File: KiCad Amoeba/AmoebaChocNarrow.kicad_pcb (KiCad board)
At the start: 2 copper layers, 12.5 x 30 mm, 10 parts, among them J1 Conn_01x01_Pin, J2 Conn_01x01_Pin, J3 Conn_01x01_Pin, J4 Conn_01x01_Pin, SW1 SW_SPST

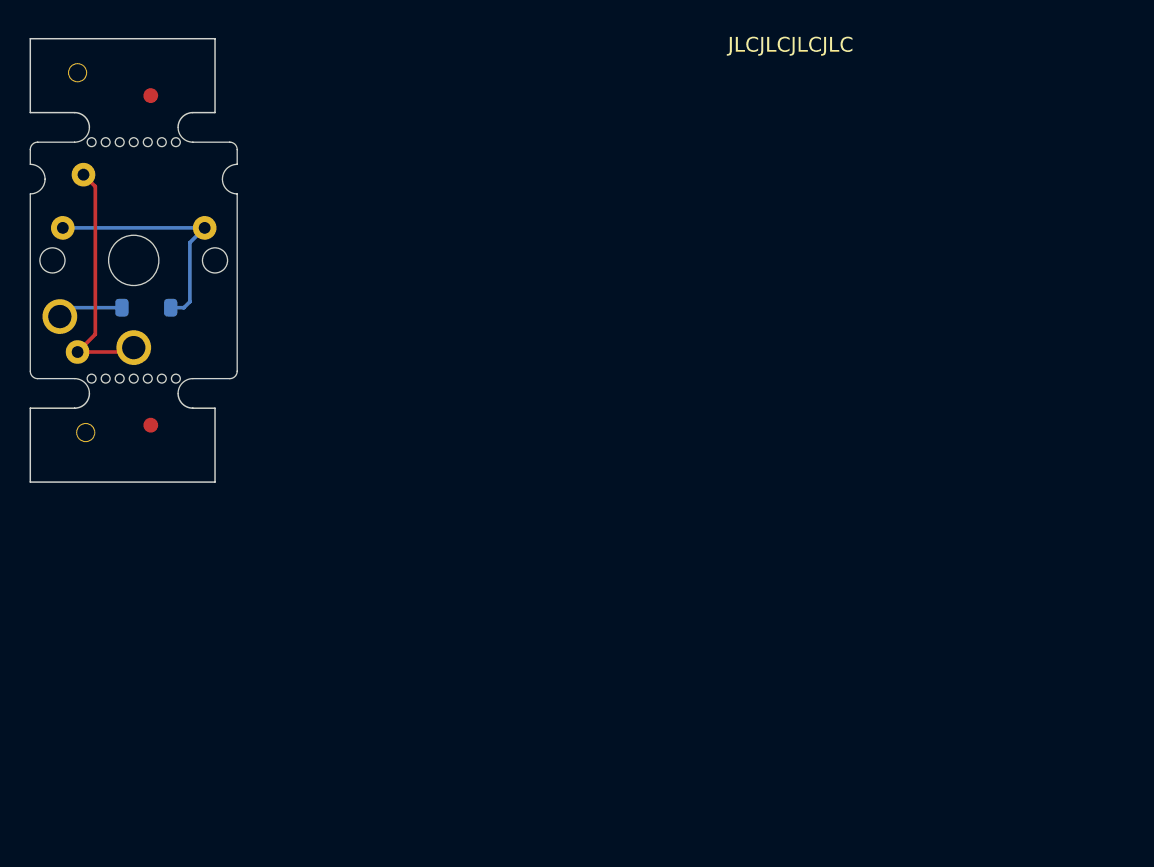
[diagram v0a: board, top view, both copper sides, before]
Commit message: feat(amoeba): clean up, hold just amoeba area
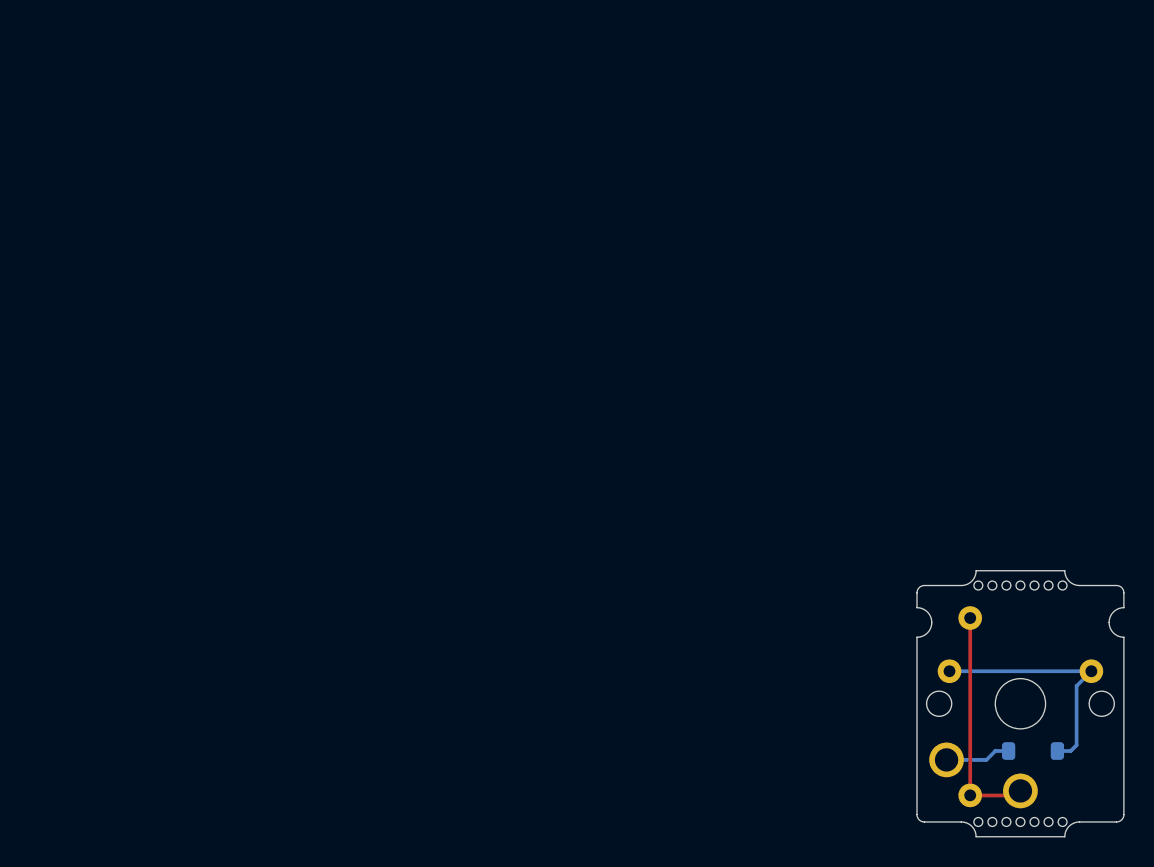
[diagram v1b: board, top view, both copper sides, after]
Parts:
- removed ? (x2): ToolingHole, Amoeba_Choc_Nar:ToolingHole_1.152mm
- removed F1 (x2): Fiducial_1mm_Mask2mm, Fiducial:Fiducial_1mm_Mask2mm
- added REF**: Mouse_Bites, Amoeba_Choc_Nar:Mouse_Bites, F.Cu at (130.0, 118.0)
- added REF**: Mouse_Bites, Amoeba_Choc_Nar:Mouse_Bites, F.Cu at (130.0, 102.0)
- moved J2 67.4 mm to (126.6, 116.2)
- moved J4 67.1 mm to (134.8, 107.8)
- moved D1 67.1 mm to (130.8, 113.2)
- moved J1 67.1 mm to (126.6, 104.2)
- moved J3 67.1 mm to (125.2, 107.8)
- moved SW1 67.1 mm to (130.0, 110.0)
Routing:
- net col: track 16.8 -> 15.5 mm
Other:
- board size 12.5 x 30 mm -> 14 x 16 mm
- board text removed: "JLCJLCJLCJLC"

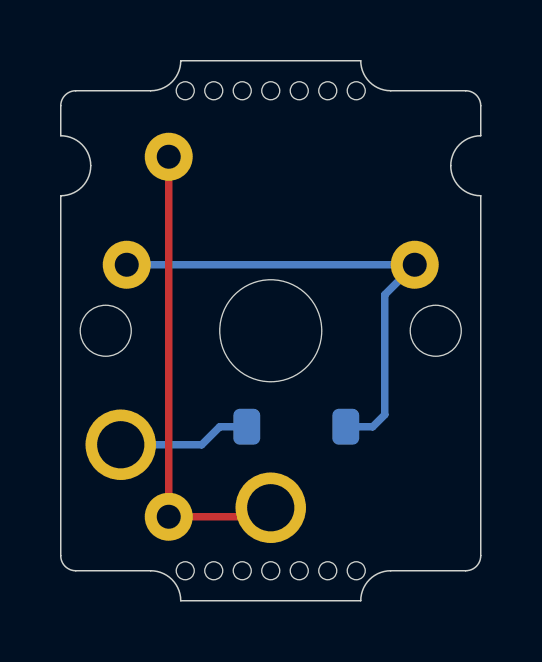
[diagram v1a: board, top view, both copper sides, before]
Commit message: feat(amoeba): cleanup
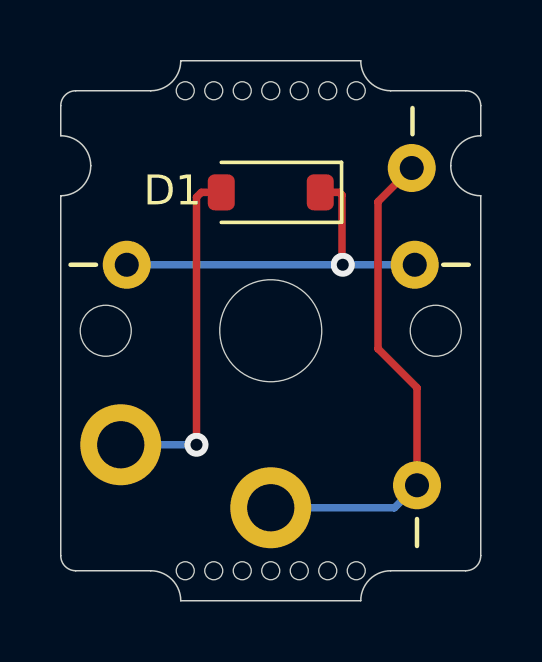
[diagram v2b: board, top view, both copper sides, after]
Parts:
- D1: moved to F.Cu
- moved J2 8.34 mm to (134.9, 115.2)
- moved J1 8.11 mm to (134.7, 104.6)
- moved D1 7.86 mm to (130.0, 105.4)
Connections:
- net col renamed /col
- net row renamed /row
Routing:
- net Net-(D1-A): track 4.45 -> 11.7 mm, vias 0 -> 1
- net /row: track 16.5 -> 12.7 mm, vias 0 -> 1
- net /col: track 15.5 -> 16.8 mm
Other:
- board text added: "Outer ticks are choc spacing, 18 x 17 Inner ticks are clip width x body depth, 14.5 x 13.8 Blue outline is switch lower body, 13.8 x 13.8"
